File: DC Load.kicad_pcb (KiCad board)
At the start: 2 copper layers, 225 x 179.3 mm, 154 parts, among them IC1 REF7050QDGKR, IC10 REF7050QDGKR, IC11 ISO7740FQDBQRQ1, IC12 ISO7741FQDBQRQ1, IC13 INA826AID, IC14 OPA210IDGKR, IC15 INA296A3IDDFR, IC16 MAX31850K, IC17 ISO7741FQDBQRQ1, IC18 ISO7741FQDBQRQ1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

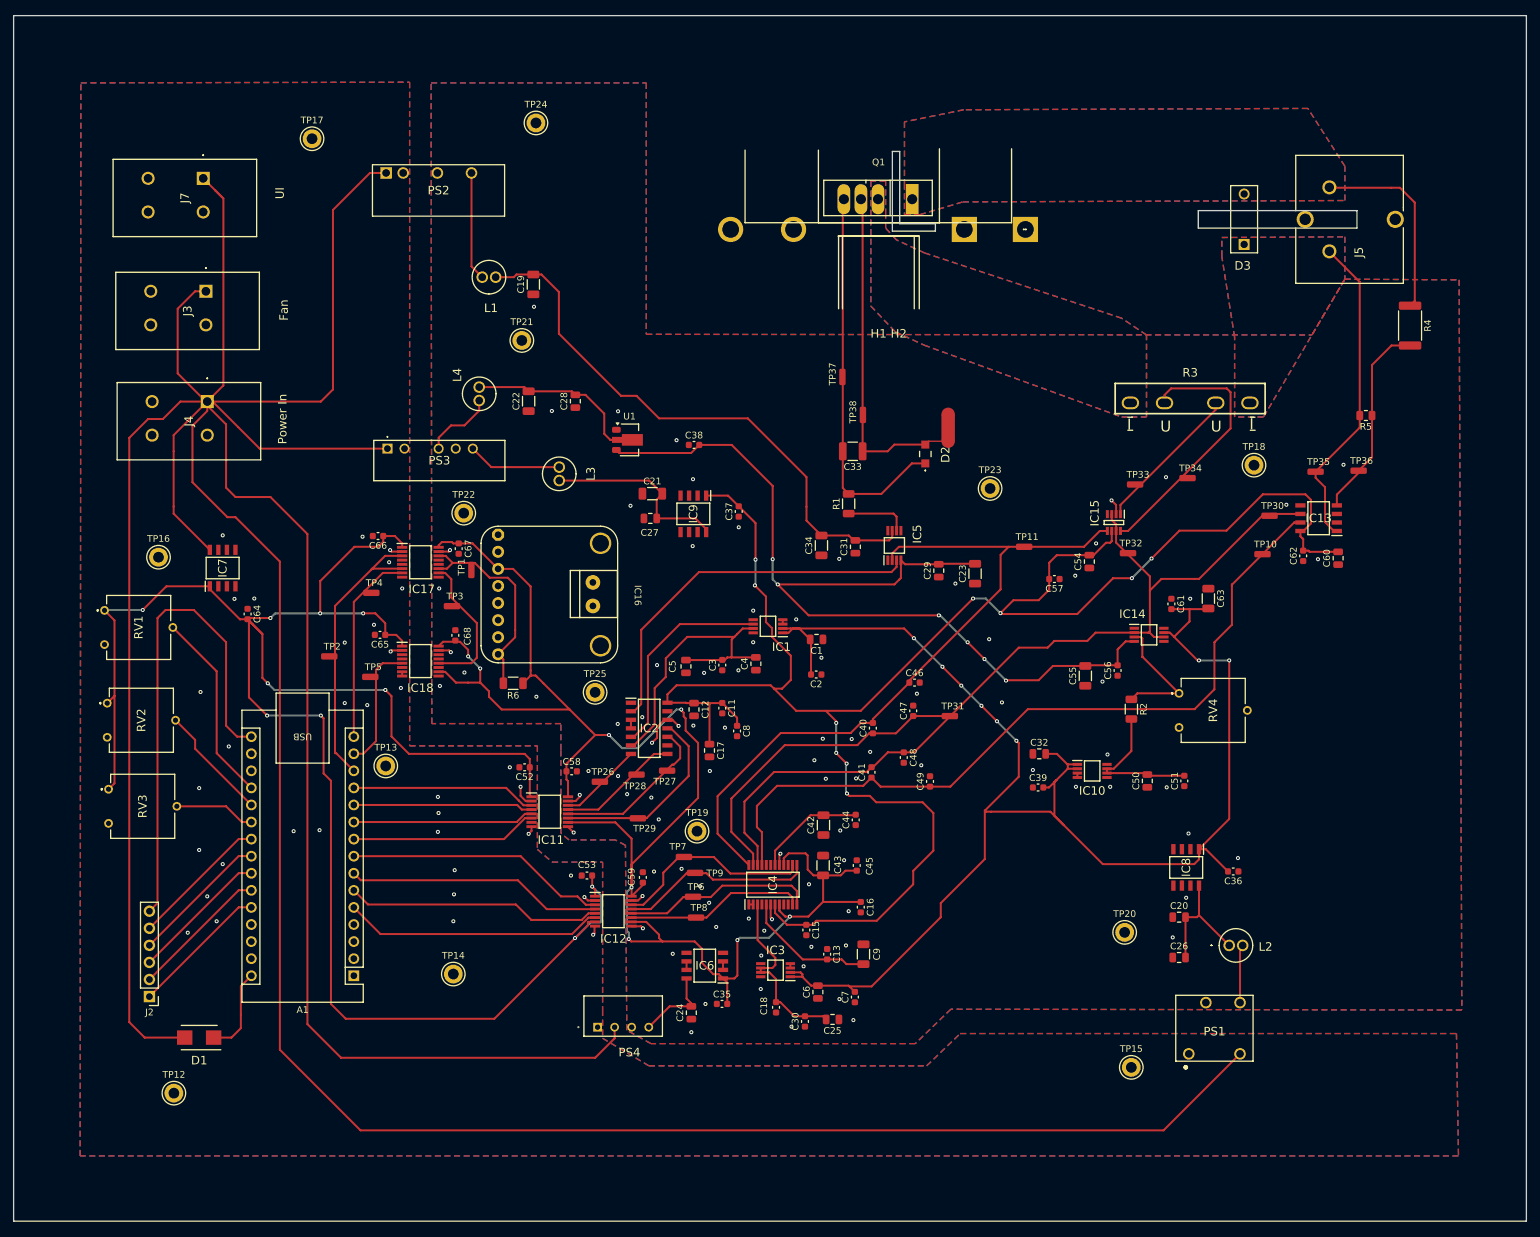
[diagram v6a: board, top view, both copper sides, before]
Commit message: added the rest of the 3D models. Added logo
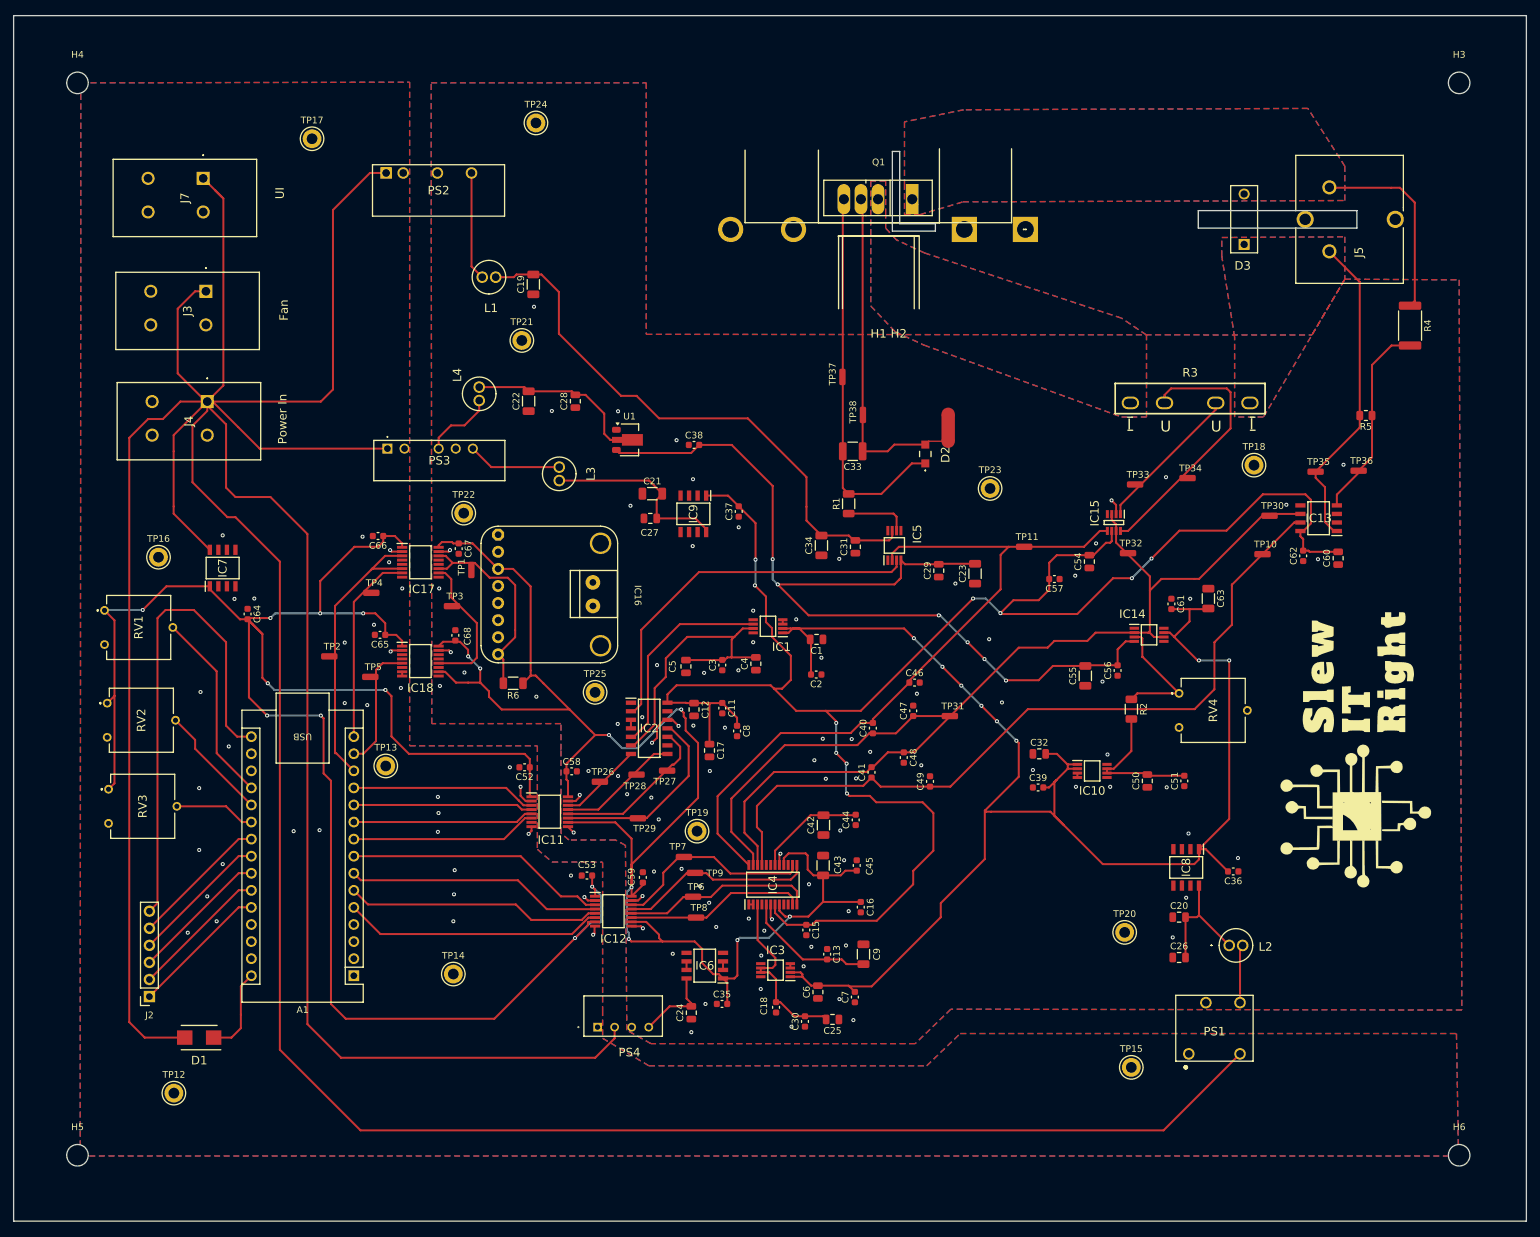
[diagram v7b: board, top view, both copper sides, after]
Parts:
- added G***: LOGO, Logos:Logos, F.Cu at (234.5, 134.5)
- added H3: MountingHole, MountingHole:MountingHole_3.2mm_M3, F.Cu at (250.0, 35.0)
- added H4: MountingHole, MountingHole:MountingHole_3.2mm_M3, F.Cu at (44.5, 35.0)
- added H5: MountingHole, MountingHole:MountingHole_3.2mm_M3, F.Cu at (44.5, 194.5)
- added H6: MountingHole, MountingHole:MountingHole_3.2mm_M3, F.Cu at (250.0, 194.5)
- J2: footprint Connector_PinHeader_2.54mm:PinHeader_1x06_P2.54mm_Vertical -> Connector_PinSocket_2.54mm:PinSocket_1x06_P2.54mm_Vertical

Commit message: small changes
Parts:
- added J1: UI, 1190363:1190363, F.Cu at (57.5, 180.0)
- J2: footprint Connector_PinSocket_2.54mm:PinSocket_1x06_P2.54mm_Vertical -> Connector_PinSocket_2.54mm:PinSocket_1x04_P2.54mm_Vertical
- moved TP12 48.7 mm to (107.5, 185.6)
- moved D1 13.6 mm to (50.5, 170.9), turned to 90 degrees
- moved J2 8.50 mm to (55.4, 162.4)
- moved H4 0.58 mm to (45.0, 34.7)
- moved H5 0.54 mm to (45.0, 194.7)
- moved H3 0.30 mm to (250.0, 34.7)
- moved H6 0.20 mm to (250.0, 194.7)
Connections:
- J2 pad 1: Net-(A1-A7) -> Net-(A1-SCL/A5)
- J2 pad 2: Net-(A1-A6) -> Net-(A1-SDA/A4)
- J2 pad 3: Net-(A1-SCL/A5) -> Net-(A1-A3)
- J2 pad 4: Net-(A1-SDA/A4) -> Net-(A1-D13/SCK)
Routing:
- net Net-(A1-VIN): track 13.1 -> 41.0 mm
- net +12V: track 688.5 -> 674.1 mm
- net Net-(A1-A6): track 20.9 -> 31.5 mm
- net Net-(A1-A7): track 20.9 -> 25.6 mm
- net +6V Isolated: track 228.1 -> 224.2 mm
- net Net-(A1-D13/SCK): track 73.6 -> 70.1 mm
- net Net-(A1-SDA/A4): track 20.9 -> 19.1 mm
- net Net-(A1-SCL/A5): track 20.9 -> 19.1 mm
- net Net-(A1-A3): track 20.9 -> 19.1 mm
- net GND: vias 35 -> 32
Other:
- board size 225 x 179.3 mm -> 225 x 180 mm
